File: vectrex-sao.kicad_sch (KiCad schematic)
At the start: 116 parts, among them U1 PIC16F886-IP, U2 IS31FL3731-SALS2, U3 NCP1117-3.3_SOT223

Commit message: initial commit
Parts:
- removed C2-10, C2-11, C2-12, C2-13, C2-14, C2-8, C2-9, C3-10, C3-11, C3-12, C3-13, C3-14, C3-8, C3-9, C4-10, C4-11, C4-12, C4-13, C4-14, C4-8, C4-9, C5-10, C5-11, C5-12, C5-13, C5-14, C5-8, C5-9, C6-10, C6-11, C6-12, C6-13, C6-14, C6-8, C6-9: LED0603_NOOUTLINE, Capacitor_SMD:C_0603_1608Metric, symbol vectrex-sao-eagle-import:LED0603_NOOUTLINE

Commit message: 4 hours of work redone in 1 hour
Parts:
- removed MS1: FEATHERWING, vectrex-sao:FEATHERWING, symbol vectrex-sao-eagle-import:FEATHERWING
- removed U3: NCP1117-3.3_SOT223, Package_TO_SOT_SMD:SOT-223-3_TabPin2, symbol Regulator_Linear:NCP1117-3.3_SOT223
- added J1: ICSP, symbol Connector_Generic:Conn_01x06
- added J2: Badgelife_sao_connector_v169bis, vectrex-sao:Badgelife-SAOv169-SAO-2x3, symbol Badgelife:Badgelife_sao_connector_v169bis
- C1, C2, C3: footprint vectrex-sao:0805-NO -> Capacitor_SMD:C_0805_2012Metric
- C1-1: footprint Capacitor_SMD:C_0603_1608Metric -> vectrex-sao:C_0603_1608Metric; symbol vectrex-sao-eagle-import:LED0603_NOOUTLINE -> vectrex-sao:LED
- C1-2, C1-3, C1-4, C1-5, C1-6, C1-7, C2-1, C2-2, C2-3, C2-4, C2-5, C2-6, C2-7, C3-1, C3-2, C3-3, C3-4, C3-5, C3-6, C3-7, C4-1, C4-2, C4-3, C4-4, C4-5, C4-6, C4-7, C5-1, C5-2, C5-3, C5-4, C5-5, C5-6, C5-7, C6-1, C6-2, C6-3, C6-4, C6-5, C6-6, C6-7, C7-1, C7-10, C7-11, C7-12, C7-13, C7-14, C7-2, C7-3, C7-4, C7-5, C7-6, C7-7, C7-8, C7-9, C8-1, C8-10, C8-11, C8-12, C8-13, C8-14, C8-2, C8-3, C8-4, C8-5, C8-6, C8-7, C8-8, C8-9: symbol vectrex-sao-eagle-import:LED0603_NOOUTLINE -> vectrex-sao:LED
- R1: footprint vectrex-sao:RESPACK_4X0603 -> vectrex-sao:R_Array_Convex_4x0603_CAT16-F4
- SJ1: footprint vectrex-sao:SOLDERJUMPER_ARROW_NOPASTE -> vectrex-sao:SolderJumper-2_P1.3mm_Open_RoundedPad1.0x1.5mm
- U2: footprint vectrex-sao:QFN28_4MM_0.4MM -> Package_DFN_QFN:QFN-28-1EP_4x4mm_P0.4mm_EP2.3x2.3mm
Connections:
- net VCC is gone; now on net +3.3V: C1.1, C2.1, C3.1, R1.7 (2), R1.8 (2), SJ1.2, U2.2 (VCC), U2.3 (SHUTDOWN)
- net CA1: now also C1-1.1 (K), C1-2.1 (K), C1-3.1 (K), C1-4.1 (K), C1-5.1 (K), C1-6.1 (K), C1-7.1 (K); no longer C1-1.C, C1-2.C, C1-3.C, C1-4.C, C1-5.C, C1-6.C, C1-7.C
- net CA2: now also C2-1.1 (K), C2-2.1 (K), C2-3.1 (K), C2-4.1 (K), C2-5.1 (K), C2-6.1 (K), C2-7.1 (K), C3-1.2 (A), C4-1.2 (A), C5-1.2 (A), C6-1.2 (A), C7-1.2 (A), C8-1.2 (A); no longer C2-1.C, C2-2.C, C2-3.C, C2-4.C, C2-5.C, C2-6.C, C2-7.C, C3-1.A, C4-1.A, C5-1.A, C6-1.A, C7-1.A, C8-1.A
- net CA3: now also C1-1.2 (A), C2-1.2 (A), C3-1.1 (K), C3-2.1 (K), C3-3.1 (K), C3-4.1 (K), C3-5.1 (K), C3-6.1 (K), C3-7.1 (K), C4-2.2 (A), C5-2.2 (A), C6-2.2 (A), C7-2.2 (A), C8-2.2 (A); no longer C1-1.A, C2-1.A, C3-1.C, C3-2.C, C3-3.C, C3-4.C, C3-5.C, C3-6.C, C3-7.C, C4-2.A, C5-2.A, C6-2.A, C7-2.A, C8-2.A
- net CA4: now also C1-2.2 (A), C2-2.2 (A), C3-2.2 (A), C4-1.1 (K), C4-2.1 (K), C4-3.1 (K), C4-4.1 (K), C4-5.1 (K), C4-6.1 (K), C4-7.1 (K), C5-3.2 (A), C6-3.2 (A), C7-3.2 (A), C8-3.2 (A); no longer C1-2.A, C2-2.A, C3-2.A, C4-1.C, C4-2.C, C4-3.C, C4-4.C, C4-5.C, C4-6.C, C4-7.C, C5-3.A, C6-3.A, C7-3.A, C8-3.A
- net CA5: now also C1-3.2 (A), C2-3.2 (A), C3-3.2 (A), C4-3.2 (A), C5-1.1 (K), C5-2.1 (K), C5-3.1 (K), C5-4.1 (K), C5-5.1 (K), C5-6.1 (K), C5-7.1 (K), C6-4.2 (A), C7-4.2 (A), C8-4.2 (A); no longer C1-3.A, C2-3.A, C3-3.A, C4-3.A, C5-1.C, C5-2.C, C5-3.C, C5-4.C, C5-5.C, C5-6.C, C5-7.C, C6-4.A, C7-4.A, C8-4.A
- net CA6: now also C1-4.2 (A), C2-4.2 (A), C3-4.2 (A), C4-4.2 (A), C5-4.2 (A), C6-1.1 (K), C6-2.1 (K), C6-3.1 (K), C6-4.1 (K), C6-5.1 (K), C6-6.1 (K), C6-7.1 (K), C7-5.2 (A), C8-5.2 (A); no longer C1-4.A, C2-4.A, C3-4.A, C4-4.A, C5-4.A, C6-1.C, C6-2.C, C6-3.C, C6-4.C, C6-5.C, C6-6.C, C6-7.C, C7-5.A, C8-5.A
- net CA7: now also C1-5.2 (A), C2-5.2 (A), C3-5.2 (A), C4-5.2 (A), C5-5.2 (A), C6-5.2 (A), C7-1.1 (K), C7-2.1 (K), C7-3.1 (K), C7-4.1 (K), C7-5.1 (K), C7-6.1 (K), C7-7.1 (K), C8-6.2 (A); no longer C1-5.A, C2-5.A, C3-5.A, C4-5.A, C5-5.A, C6-5.A, C7-1.C, C7-2.C, C7-3.C, C7-4.C, C7-5.C, C7-6.C, C7-7.C, C8-6.A
- net CA8: now also C1-6.2 (A), C2-6.2 (A), C3-6.2 (A), C4-6.2 (A), C5-6.2 (A), C6-6.2 (A), C7-6.2 (A), C8-1.1 (K), C8-2.1 (K), C8-3.1 (K), C8-4.1 (K), C8-5.1 (K), C8-6.1 (K), C8-7.1 (K); no longer C1-6.A, C2-6.A, C3-6.A, C4-6.A, C5-6.A, C6-6.A, C7-6.A, C8-1.C, C8-2.C, C8-3.C, C8-4.C, C8-5.C, C8-6.C, C8-7.C
- net CA9: now also C1-7.2 (A), C2-7.2 (A), C3-7.2 (A), C4-7.2 (A), C5-7.2 (A), C6-7.2 (A), C7-7.2 (A), C8-7.2 (A); no longer C1-7.A, C2-7.A, C3-7.A, C4-7.A, C5-7.A, C6-7.A, C7-7.A, C8-7.A
- net CB1: now also C7-8.2 (A), C8-8.2 (A); no longer C7-8.A, C8-8.A
- net CB2: now also C7-9.2 (A), C8-9.2 (A); no longer C7-9.A, C8-9.A
- net CB3: now also C7-10.2 (A), C8-10.2 (A); no longer C7-10.A, C8-10.A
- net CB4: now also C7-11.2 (A), C8-11.2 (A); no longer C7-11.A, C8-11.A
- net CB5: now also C7-12.2 (A), C8-12.2 (A); no longer C7-12.A, C8-12.A
- net CB6: now also C7-13.2 (A), C8-13.2 (A); no longer C7-13.A, C8-13.A
- net CB7: now also C7-10.1 (K), C7-11.1 (K), C7-12.1 (K), C7-13.1 (K), C7-14.1 (K), C7-8.1 (K), C7-9.1 (K), C8-14.2 (A); no longer C7-10.C, C7-11.C, C7-12.C, C7-13.C, C7-14.C, C7-8.C, C7-9.C, C8-14.A
- net CB8: now also C7-14.2 (A), C8-10.1 (K), C8-11.1 (K), C8-12.1 (K), C8-13.1 (K), C8-14.1 (K), C8-8.1 (K), C8-9.1 (K); no longer C7-14.A, C8-10.C, C8-11.C, C8-12.C, C8-13.C, C8-14.C, C8-8.C, C8-9.C
- net GND: now also U1.19 (VSS), U1.8 (VSS), J1.3 (Pin_3), J2.2 (GND)
- net SCL: now also U1.14 (RC3/SCK/SCL), J2.4 (SCL)
- net SDA: now also U1.15 (RC4/SDI/SDA), J2.3 (SDA)
- net n_MCLR: now reaches U1.1 (RE3/~{MCLR}/Vpp)
- net n_MCLR: now also J1.1 (Pin_1)
- net +3.3V: now reaches U1.20 (VDD)
- net +3.3V: now also J1.2 (Pin_2), J2.1 (VCC)
- net ICSPCLK: now reaches U1.27 (ICSPCLK/RB6)
- net ICSPCLK: now also J1.5 (Pin_5)
- net ICSPDAT: now reaches U1.28 (ICSPDAT/RB7)
- net ICSPDAT: now also J1.4 (Pin_4)
- new net MISO: J2.5 (GPIO1)
- new net SCLK: J2.6 (GPIO2)
- no-connect marks 0 -> 4
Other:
- note added: "TODO"
- moved on the sheet: C1, C2, C3, R1A, R1B, R1C, R1D, SJ1, U2

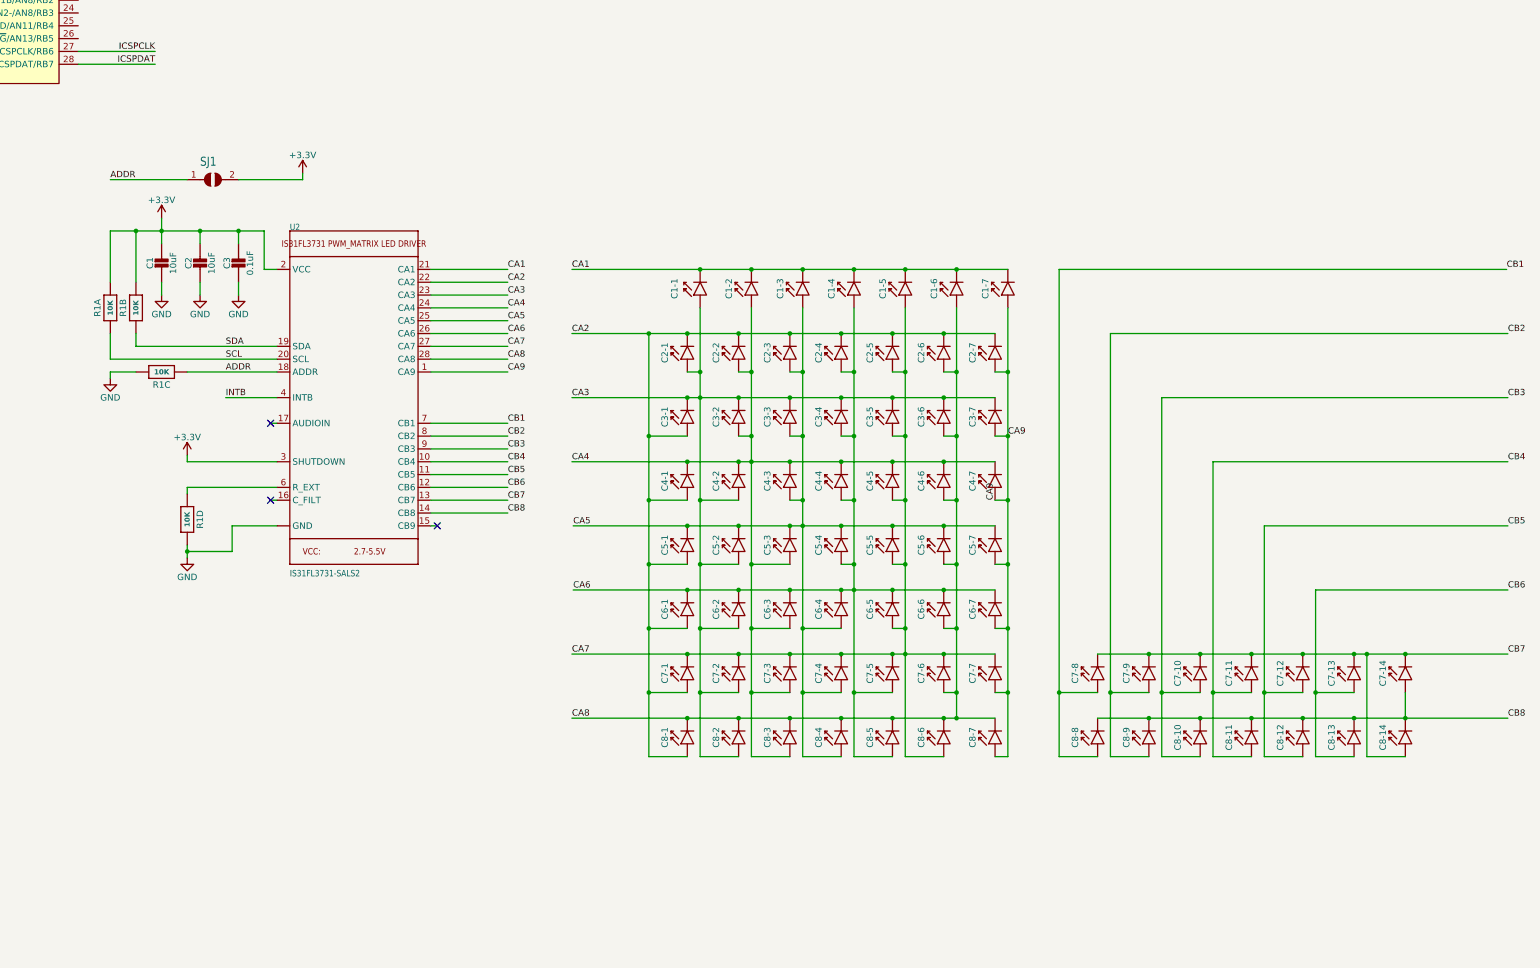
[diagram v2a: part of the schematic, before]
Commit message: rearrange the bottom two rows
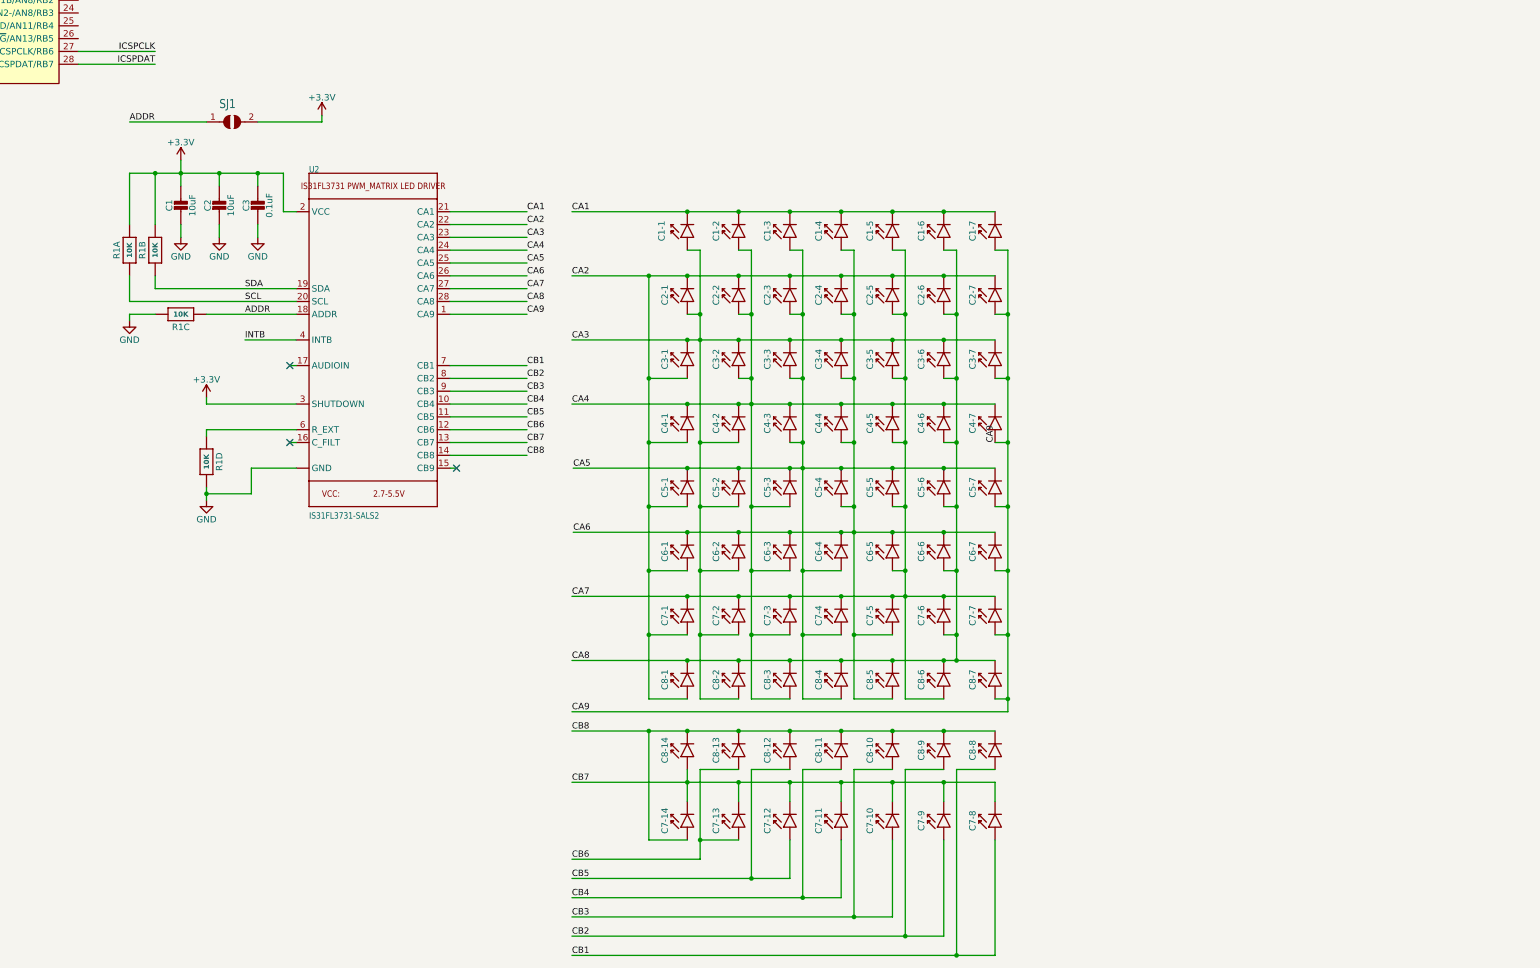
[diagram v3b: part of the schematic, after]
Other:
- moved on the sheet: C1, C1-1, C1-2, C1-3, C1-4, C1-5, C1-6, C1-7, C2, C2-1, C2-2, C2-3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

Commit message: finished outline, added controller board
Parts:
- removed FID1: FIDUCIAL{dblquote}{dblquote}, vectrex-sao:FIDUCIAL_1MM, symbol vectrex-sao-eagle-import:FIDUCIAL{dblquote}{dblquote}
- removed SJ1: SOLDERJUMPER, vectrex-sao:SolderJumper-2_P1.3mm_Open_RoundedPad1.0x1.5mm, symbol vectrex-sao-eagle-import:SOLDERJUMPER
- added C4: 0.1uF, Capacitor_SMD:C_0805_2012Metric, symbol vectrex-sao:CAP_CERAMIC0805-NOOUTLINE
- added C5: 0.1uF, Capacitor_SMD:C_0603_1608Metric, symbol vectrex-sao:CAP_CERAMIC0805-NOOUTLINE
- added C6: 22pF, Capacitor_SMD:C_0603_1608Metric, symbol vectrex-sao:CAP_CERAMIC0805-NOOUTLINE
- added JP3: ADDR, vectrex-sao:SolderJumper-2_P1.3mm_Open_RoundedPad1.0x1.5mm, symbol Jumper:SolderJumper_2_Open
- added JP4: TX, vectrex-sao:SolderJumper-2_P1.3mm_Open_RoundedPad1.0x1.5mm, symbol Jumper:SolderJumper_2_Open
- added JP5: RX, vectrex-sao:SolderJumper-2_P1.3mm_Open_RoundedPad1.0x1.5mm, symbol Jumper:SolderJumper_2_Open
- added R2: 10k, Resistor_SMD:R_0603_1608Metric, symbol Device:R
- added R3: 1k, Resistor_SMD:R_0603_1608Metric, symbol Device:R
- added U3: TC233A, Package_TO_SOT_SMD:SOT-23-6, symbol vectrex-sao:TC233A
- C1, C2, C3: symbol vectrex-sao-eagle-import:CAP_CERAMIC0805-NOOUTLINE -> vectrex-sao:CAP_CERAMIC0805-NOOUTLINE
- C1-1: footprint vectrex-sao:C_0603_1608Metric -> vectrex-sao:LED_0603_1608Metric
- C1-2, C1-3, C1-4, C1-5, C1-6, C1-7, C2-1, C2-2, C2-3, C2-4, C2-5, C2-6, C2-7, C3-1, C3-2, C3-3, C3-4, C3-5, C3-6, C3-7, C4-1, C4-2, C4-3, C4-4, C4-5, C4-6, C4-7, C5-1, C5-2, C5-3, C5-4, C5-5, C5-6, C5-7, C6-1, C6-2, C6-3, C6-4, C6-5, C6-6, C6-7, C7-1, C7-10, C7-11, C7-12, C7-13, C7-14, C7-2, C7-3, C7-4, C7-5, C7-6, C7-7, C7-8, C7-9, C8-1, C8-10, C8-11, C8-12, C8-13, C8-14, C8-2, C8-3, C8-4, C8-5, C8-6, C8-7, C8-8, C8-9: footprint Capacitor_SMD:C_0603_1608Metric -> vectrex-sao:LED_0603_1608Metric
- J1: footprint (none) -> Connector_PinHeader_2.54mm:PinHeader_1x06_P2.54mm_Vertical_SMD_Pin1Right
- JP1: renamed from FID2; value FIDUCIAL{dblquote}{dblquote} -> TOUCH_PAD; footprint vectrex-sao:FIDUCIAL_1MM -> vectrex-sao:MountingHole_1.5mm_M2_Pad_TopOnly
- R1: symbol vectrex-sao-eagle-import:RESISTOR_4PACK -> vectrex-sao:RESISTOR_4PACK
- U1: symbol MCU_Microchip_PIC16:PIC16F886-IP -> vectrex-sao:PIC16F886-IP
- U2: symbol vectrex-sao-eagle-import:IS31FL3731QFN -> vectrex-sao:IS31FL3731QFN
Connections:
- net +3.3V: now also C4.1, C5.1, JP3.1 (A), R2.2, U3.4 (LHO), U3.5 (VDD)
- net ADDR: now also JP3.2 (B)
- net GND: now also U2.29 (GND), C4.2, C5.2, C6.2, U3.2 (GND), U3.6 (OHO); no longer U2.5 (GND), U2.THERMAL (GND)
- net SCL: no longer J2.4 (SCL)
- net SDA: no longer J2.3 (SDA)
- net at U1.17 (RC6/TX/CK): now also JP4.2 (B)
- net at U1.18 (RC7/RX/DT): now also JP5.2 (B)
- net TOUCH_UC: now reaches U1.21 (INT/AN12/RB0)
- net TOUCH_UC: now also R2.1, U3.1 (OUT)
- net MISO renamed RX
- net RX: now also JP5.1 (A)
- net SCLK renamed TX
- net TX: now also JP4.1 (A)
- net n_MCLR renamed MCLR
- new net: C6.1, R3.1, U3.3 (TCH)
- new net TOUCH_PAD: JP1.1 (TP), R3.2
- no-connect marks 4 -> 6
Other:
- note removed: "TODO"
- moved on the sheet: C1, C2, C3, J1, J2, R1A, R1B, R1C, R1D

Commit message: updated models and created files for ordering
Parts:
- removed unit 4 of R1
- added D1: MBR0520, Diode_SMD:D_SOD-123, symbol Diode:MBR0520
- added JP2, JP6, JP7, JP8: solderjumper-3way, vectrex-sao:SolderJumper-3_P1.3mm_Bridged12_RoundedPad1.0x1.5mm_NumberLabels, symbol Jumper:SolderJumper_3_Bridged12
- added JP9: SOUND, vectrex-sao:SolderJumper-2_P1.3mm_Open_RoundedPad1.0x1.5mm, symbol Jumper:SolderJumper_2_Open
- added LED1: LED0603_NOOUTLINE, vectrex-sao:LED_0603_1608Metric, symbol vectrex-sao:LED
- added LS1, LS2: Speaker FUET-9032-05, vectrex-sao:MagneticBuzzer_FUET-9032-05, symbol Device:Speaker
- added Q1: MMBT3904, Package_TO_SOT_SMD:SOT-23, symbol Transistor_BJT:MMBT3904
- added R4, R5: 1k, Resistor_SMD:R_0603_1608Metric, symbol Device:R
- added R6: 10k, Resistor_SMD:R_0603_1608Metric, symbol Device:R
- J1: symbol Connector_Generic:Conn_01x06 -> vectrex-sao:Conn_01x06
- J2: value Badgelife_sao_connector_v169bis -> SAO_v169bis
- JP3: value ADDR -> 0x77
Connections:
- net INTB is gone; now on net LED_INT_UC: U2.4 (INTB)
- net +3.3V: now also D1.1 (K), LS1.1, R4.2
- net GND: now also U2.5 (GND), LS2.2, Q1.2 (E), R6.1
- net TOUCH_UC: now also JP7.1 (A); no longer R2.1, U3.1 (OUT)
- net PWM_UC: now reaches U1.13 (RC2/P1A/CCP1)
- net PWM_UC: now also JP8.1 (A)
- net LED_INT_UC: now reaches U1.24 (PGM/C12IN2-/AN8/RB3)
- net at U2.6 (R_EXT): now also R6.2
- net SDA_BADGE: now reaches J2.3 (SDA)
- net SDA_BADGE: now also JP2.3 (B)
- net SCL_BADGE: now reaches J2.4 (SCL)
- net SCL_BADGE: now also JP6.3 (B)
- net RX renamed PWM_BADGE
- net PWM_BADGE: now also JP8.3 (B)
- net SCL renamed SCL_LED
- net SCL_LED: now also JP6.2 (C); no longer U1.14 (RC3/SCK/SCL)
- net SDA renamed SDA_LED
- net SDA_LED: now also JP2.2 (C); no longer U1.15 (RC4/SDI/SDA)
- net TX renamed TOUCH_BADGE
- net TOUCH_BADGE: now also JP7.3 (B)
- new net: D1.2 (A), LS1.2, Q1.3 (C)
- new net: LED1.2 (A), R4.1
- new net: JP9.2 (B), R5.1
- new net: LS2.1, Q1.1 (B), R5.2
- new net PWM_IN: JP8.2 (C), JP9.1 (A)
- new net SCL_UC: JP6.1 (A), U1.14 (RC3/SCK/SCL)
- new net SDA_UC: JP2.1 (A), U1.15 (RC4/SDI/SDA)
- new net TOUCH_OUT: JP7.2 (C), LED1.1 (K), R2.1, U3.1 (OUT)
- no-connect marks 6 -> 19
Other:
- note added: "1k for NPN driver 220 for direct drive"
- note added: "A jumper is installed to connect the joystick PCB to the TOUCH_PAD input."
- note added: "C1-1 . . . C1-7 . . . C7-14 . . . C7-8"
- note added: "Connect only one!!"
- note added: "Currently no UART supported in PIC FW. Proposed feature is realtime text scrolling from rcv'd characters."
- note added: "R5 & LS2 for quieter operation. R5, Q1, D1, LS1 for loud operation!"
- note added: "Who's in charge?? PIC or BADGE"
- company: (none) -> https://www.PlayVectrex.com
- title: Vectrex SAO -> Vectrex SAO by Brett Walach
- moved on the sheet: C4, C5, C6, JP4, JP5, R2, R3, U3
